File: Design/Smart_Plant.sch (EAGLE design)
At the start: 85 parts, among them IC1 NE555D, Q1 IRLML0100, Q3 2.5A/30V, Q4 MBT3904DW1T1, U10 ESP3212, U6 W25Q32FVSS, U7 FT231XS, U8 MCP73831, U9 AP2112K-3.3V, X2 MICROSD, Y3 26MHz

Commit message: Updated design files for Smart_Plant
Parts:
- removed C29, C30: 10pF, SparkFun-Capacitors:10PF-0603-50V-5%
- removed C31, C32: 270pF, esp32-thing-temp:270PF-50V-5%(0603)
- removed C33: 10nF, SparkFun-Capacitors:10NF-0603-50V-10%
- removed C34, C37, C38, C41, C48, C49, C51, C53: 0.1uF, SparkFun-Capacitors:0.1UF-0603-25V-(+80/-20%)
- removed C35: 2.4pF, esp32-thing-temp:2.4PF-0603-50V-5%
- removed C36: 5.6pF, esp32-thing-temp:5.6PF-50V-5%(0603)
- removed C39, C40: 47pF, SparkFun-Capacitors:47PF-0603-50V-5%
- removed C42: 4.7uF, SparkFun-Capacitors:4.7UF-6.3V-10%(0603)0603
- removed C43: 1.0uF, SparkFun-Capacitors:1.0UF-0805-25V-(+80/-20%)
- removed C44: 2.2uF, SparkFun-Capacitors:2.2UF-0603-10V-20%
- removed C45, C46: 4.7uF, SparkFun-Capacitors:4.7UF0603
- removed C47: 100pF, SparkFun-Capacitors:100PF-0603-50V-5%
- removed C50: 10uF, SparkFun-Capacitors:10UF-0603-6.3V-20%
- removed C52: 1.0uF, SparkFun-Capacitors:1.0UF-0603-16V-10%
- removed C56: 3.0nF, esp32-thing-temp:3.0NF-0603-50V-5%
- removed D10, D9: MBR0530, microbuilder:DIODE-SCHOTTKYSOD-123
- removed D5: BAT20J, SparkFun-DiscreteSemi:DIODE-SCHOTTKY-BAT20J
- removed D6: Yellow, SparkFun-LED:LED-YELLOW0603
- removed D7: Green, SparkFun-LED:LED-RED0603
- removed E2: ANTENNA, esp32-thing-temp:ANTENNATRACE-TUNED
- removed EINK1: EINK_24PIN_290IN, microbuilder:EINK_24PIN_290IN
- removed F2: 500mA, SparkFun-PowerIC:PTCSMD
- removed JP1: (no value), SparkFun-Connectors:USB_MICROB_PLUGCONN-11752
- removed JP3: LiPo, SparkFun-Connectors:M02JST-PTH-2
- removed L2: 2.7nH, SparkFun-Passives:INDUCTOR0603
- removed Q3: 2.5A/30V, SparkFun-DiscreteSemi:MOSFET-PCHANNELDMG2307L
- removed Q4: MBT3904DW1T1, esp32-thing-temp:MBT3904DW1T1
- removed R19, R24: 1K, SparkFun-Resistors:1KOHM-1/10W-1%(0603)
- removed R20: 2.0k, SparkFun-Resistors:2.0KOHM1/10W5%(0603)
- removed R21: DNP, SparkFun-Passives:RESISTORPTH-1/6W
- removed R22, R23: 10k, SparkFun-Resistors:10KOHM-0603-1/10W-1%
- removed R26: 10k, SparkFun-Resistors:10KOHM-1/10W-1%(0603)0603
- removed R27: DNP, microbuilder:RESISTOR0805_10MGAP
- removed S3: RESET, SparkFun-Electromechanical:SWITCH-MOMENTARY-2SMD-4.6X2.8MM
- removed S4: BTN-0, SparkFun-Electromechanical:SWITCH-MOMENTARY-2SMD-4.6X2.8MM
- removed SJ4: JUMPER-PAD-3-2OF3_NC_BY_TRACE_SMALL, SparkFun-Passives:JUMPER-PAD-3-2OF3_NC_BY_TRACE_SMALL
- removed SJ5: JUMPER-PAD-2-NC_BY_TRACE, SparkFun-Passives:JUMPER-PAD-2-NC_BY_TRACE
- removed U10: ESP3212, esp32-thing-temp:ESP3212
- removed U6: W25Q32FVSS, SparkFun-DigitalIC:W25Q32FVSS
- removed U7: FT231XS, SparkFun-DigitalIC:FT231XS
- removed U8: MCP73831, SparkFun-PowerIC:MCP73831
- removed U9: AP2112K-3.3V, SparkFun-PowerIC:V_REG_LDOSMD
- removed X2: MICROSD, microbuilder:MICROSD
- removed Y3: 26MHz, things:CRYSTAL-GROUNDED3.2X2.5
- added BT1: (no value), SparkFun-Batteries:BATTERY-20MM_PTH
- added C10, C16, C4: 10uF, rcl:C-USC0603
- added C11, C6: 100nF, rcl:C-USC0603
- added C12: 22uF, rcl:C-USC0603
- added C15: 0.1uF, rcl:C-USC0603
- added C5: 10nF, rcl:C-USC0603
- added C7: 1uF, rcl:C-USC0603
- added D1, D2, D3: SS14, SparkFun-DiscreteSemi:DIODE-SCHOTTKY-SS14
- added FPC: E-PAPER-FPC, SpaceDIY_connectors:E-PAPER-FPC
- added IC2: TLC555CDR, linear:NE555D
- added IC3: AHT20, SamacSys_Parts:AHT20
- added IC4: TP4056, TP4056:TP4056
- added J1: (no value), SparkFun-Connectors:CONN_02
- added J3: (no value), pinhead:PINHD-1X4
- added LED1: Red, SpaceDIY_semiconductors:LED0603
- added LED2: Green, SpaceDIY_semiconductors:LED0603
- added Q2: ALS-PT19-315C, SparkFun-DiscreteSemi:PHOTOTRANSISTORPT17-21C-L41-TR8
- added R14, R7: 10k, rcl:R-US_R0603
- added R17: 220, rcl:R-US_R0603
- added R4: 33k, rcl:R-US_R0603
- added R5: 1K, rcl:R-US_R0603
- added R6: 1k, rcl:R-US_R0603
- added R8: 1M, rcl:R-US_R0603
- added R9: 10K, rcl:R-US_R0603
- added S1: Flash, SpaceDIY_electromechanical:MOMENTARY-SWITCH-SPST-SMD-5.2MM-TALL
- added S2: Reset, SpaceDIY_electromechanical:MOMENTARY-SWITCH-SPST-SMD-5.2MM-TALL
- added T1: MMBT2222A, JLC PCB Basic Parts_loc:T_NPN_MMBT2222A-1P_CHANGJ_SOT23-BEC
- added T2: LBSS84LT1G, JLC PCB Basic Parts_loc:T_P-MOSFET_LBSS84LT1G_LRC_SOT23-GSD
- added TP1, TP2: TPB1,27, testpad:TPB1,27
- added U1: ESP-32S, esp32:ESP-32S
- C1: value 0.1uF -> 10uF; device SparkFun-Capacitors:0.1UF-0603-25V-(+80/-20%) -> rcl:C-USC0603
- C13, C14, C17, C18, C19, C25, C27, C28, C9: device microbuilder:CAP_CERAMIC0805-NOOUTLINE -> rcl:C-USC0603
- C2: value 0.1uF -> 4.7uF; device SparkFun-Capacitors:0.1UF-0603-25V-(+80/-20%) -> rcl:C-USC0603
- C26: value 4.7uF/25V -> 4.7uF; device microbuilder:CAP_CERAMIC0805-NOOUTLINE -> rcl:C-USC0603
- C3: value 0.1uF -> 0.47nF; device SparkFun-Capacitors:0.1UF-0603-25V-(+80/-20%) -> rcl:C-USC0603
- C8: value 10uF/10V+ -> 10uF; device microbuilder:CAP_CERAMIC0805-NOOUTLINE -> rcl:C-USC0603
- D4: value MBR0530 -> LL4148; device microbuilder:DIODE-SCHOTTKYSOD-123 -> SpaceDIY_semiconductors:LL4148
- IC1: value NE555D -> AMS1117-3.3; device linear:NE555D -> SparkFun-IC-Power:V_REG_LD1117VXXLD1117-SMD
- R1, R12, R15: value 27 -> 10k; device SparkFun-Resistors:27OHM1/10W1%(0603)0603-RES -> rcl:R-US_R0603
- R10: device SparkFun-Resistors:10KOHM-1/10W-1%(0603)0603 -> rcl:R-US_R0603
- R11: value 20k -> 1k; device SparkFun-Resistors:20KOHM-0603-1/10W-1% -> rcl:R-US_R0603
- R13: value 0.47ohm -> 0.47; device microbuilder:RESISTOR0805_10MGAP -> rcl:R-US_R0603
- R16: device SparkFun-Resistors:10KOHM-0603-1/10W-1% -> rcl:R-US_R0603
- R2: value 27 -> 330R; device SparkFun-Resistors:27OHM1/10W1%(0603)0603-RES -> rcl:R-US_R0603
- R3: value 27 -> 1.5k; device SparkFun-Resistors:27OHM1/10W1%(0603)0603-RES -> rcl:R-US_R0603
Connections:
- removed net 0: Q4Q2.C, R26.1, S4.2, U10.(ADC2:1/TOUCH1/RTC11/CLK_OUT1)GPIO0
- removed net 12: U10.(GPIO12/ADC2:5/TOUCH5/RTC15/SPIQ)MTDI
- removed net 19: U10.(VSPIQ/HS2_DATA2)GPIO19
- removed net 21: U10.(VSPIHD/HS2_CMD)GPIO21
- removed net 22: U10.(VSPIWP/HS2_CLK)GPIO22
- removed net 25: U10.(DAC1/ADC2:8/RTC6)GPIO25
- removed net 26: U10.(DAC2/ADC2:9/RTC7)GPIO26
- removed net 27: U10.(ADC2:7/TOUCH7/RTC17)GPIO27
- removed net 3.3V_F: C41.1, U7.!RESET, U7.3V3OUT, U7.VCCIO
- removed net 32: U10.32K_XP(GPIO32/ADC1:4/TOUCH9/RTC9)
- removed net 33: U10.32K_XN(GPIO33/ADC1:5/TOUCH8/RTC8)
- removed net 34: U10.VDET_1(GPI34/ADC1:6)
- removed net 35: U10.VDET_2(GPI35/ADC1:7)
- removed net 36: C31.2, U10.SENSOR_VP(GPI36/ADC1:0/RTC0)
- removed net 37: C31.1, U10.SENSOR_CAPP(GPI37/ADC1:1/RTC1)
- removed net 38: C32.1, U10.SENSOR_CAPN(GPI38/ADC1:2/RTC2)
- removed net 39: C32.2, U10.SENSOR_VN(GPI39/ADC1:3/RTC3)
- removed net 3V3: C44.1, C47.1, C48.1, C49.1, C50.1, C51.1, C53.1, C8.2, EINK1.VCI, EINK1.VDDIO, L3.2, R10.2, R24.1, R26.2, SJ4.3, U10.VDD3P3_CPU, U10.VDD3P3_RTC, U10.VDDA, U10.VDDA3P3, U9.OUT, X2.SD_VDD
- removed net CAP_10N1: C33.2, C56.1, R11.2, U10.CAP1
- removed net CHIP_PU: Q4Q1.C, R10.1, S3.2, U10.CHIP_PU
- removed net D+: C39.1, JP1.D+, R15.1
- removed net D-: C40.1, JP1.D-, R12.1
- removed net DTR: Q4Q2.E, R22.1, U7.!DTR
- removed net FLASH_SCK: U10.(GPIO6/SPICLK/HS1_CLK/U1CTS)SD_CLK, U6.SCK
- removed net FLASH_SCS: U10.(GPIO11/SPICSO/HS1_CMD/U1RTS)SD_CMD, U6.!CS!
- removed net FLASH_SDI: U10.(GPIO8/SPID/HS1_DATA1)SD_DATA1, U6.SI(D0)
- removed net FLASH_SDO: U10.(GPIO7/SPI1/HS1_DATA0)SD_DATA0, U6.SO(D1)
- removed net FLASH_SHD: U10.(GPIO9/SPIHD/HS1_DATA2/U1RX)SD_DATA2, U6.!HOLD!(D3)
- removed net FLASH_SWP: U10.(GPIO10/SPIWP/HS1_DATA3/U1TX)SD_DATA3, U6.!WP!(D2)
- removed net FLASH_VDD: C52.1, SJ4.1, U10.VDD3P3_SDIO
- removed net LNA_IN1: C36.1, L2.1, U10.LNA_IN
- removed net MISO_SD: U10.(ADC2:2/TOUCH2/RTC12/SPIWP)GPIO2, X2.DATA_OUT
- removed net MOSI_SD: U10.(GPIO15/ADC2:3/TOUCH3/RTC13/SPICSO/U0RTS)MTDO, X2.DATA_IN
- removed net N$19: D6.A, R19.2
- removed net N$20: D6.C, U8.STAT
- removed net N$21: R21.2, SJ5.2, U8.PROG
- removed net N$22: R20.2, SJ5.1
- removed net N$23: Q4Q1.B, R22.2
- removed net N$24: Q4Q2.B, R23.2
- removed net N$25: C29.2, U10.XTAL_P, Y3.1
- removed net N$26: C30.2, U10.XTAL_N, Y3.2
- removed net N$27: D7.A, R24.2
- removed net N$30: C56.2, R11.1, U10.CAP2
- removed net RTS: Q4Q1.E, R23.1, U7.!RTS
- removed net SCLK_SD: U10.(GPIO14/ADC2:6/TOUCH6/RTC16/SPICLK)MTMS, X2.SCLK
- removed net SDCS_SD: U10.(GPIO13/ADC2:4/TOUCH4/RTC14/SPID/U0CTS)MTCK, X2.CS
- removed net SHIELD: JP1.SHIELD
- removed net TRACE_ANT1: C35.1, C36.2, E2.SIGNAL
- removed net TSCL: EINK1.TSCL
- removed net TSDA: EINK1.TSDA
- removed net U0RXD: U10.(GPIO3/CLK_OUT2/HS2_DATA0)U0RXD, U7.TXD
- removed net U0TXD: U10.(GPIO1/CLK_OUT3/HS2_DATA1)U0TXD, U7.RXD
- removed net VUSB-RAW: C37.1, F2.1, JP1.VCC
- removed net V_BATT: C45.1, JP3.2, Q3.D, U8.VBAT
- removed net V_USB: C38.1, C42.1, C46.1, D5.A, F2.2, Q3.G, R16.2, R19.1, U7.VCC, U8.VIN
- new net 3.3V: C10.1, C11.1, C12.1, C2.1, FPC.15, FPC.16, IC1.OUT, J3.1, L3.2, R10.1, R12.1, R9.2, T2.S, U1.3V3
- new net IO0: R12.2, S1.2, U1.IO0
- new net LIGHT: Q2.E, R14.1, U1.IO33
- new net MOISTURE: C7.1, D4.C, R8.1, U1.IO32
- new net N$1: IC4.PROG, R4.2
- new net N$10: C15.1, C16.1, IC3.VDD, R17.2
- new net N$2: IC4.!STDBY, R6.2
- new net N$3: LED1.C, R5.1
- new net N$4: LED2.C, R6.1
- new net N$7: IC2.DIS, R2.2, R3.1
- new net N$8: C5.2, IC2.CV
- new net N$9: R10.2, T1.C, T2.G
- new net OUT: IC2.Q, R7.2, TP1.TP
- new net PROBE: D4.A, R7.1
- new net RST: R9.1, S2.2, U1.EN
- new net RX: J3.4, U1.U0RXD
- new net SCL: IC3.SCL, R15.2, U1.IO22
- new net SDA: IC3.SDA, R16.2, U1.IO21
- new net SENS: R11.1, U1.IO16
- new net TX: J3.3, U1.U0TXD
- new net VBAT: BT1.+, C4.1, C8.1, IC1.IN, IC4.BAT
- new net VSENS: C6.1, IC2.R, IC2.V+, Q2.C, R15.1, R16.1, R17.1, R2.1, T2.D, TP2.TP
- net BUSY: now also FPC.9, U1.IO25; no longer EINK1.BUSY, U10.(ADC2:0/TOUCH0/RTC10/SPIHD)GPIO4
- net DC: now also FPC.11, U1.IO27; no longer EINK1.D/C#, U10.(HS1_DATA5)GPIO17
- net DISPCS: now also FPC.12, U1.IO15; no longer EINK1.CS#, U10.(VSPICS0/HS1_DATA6)GPIO5
- net GDR: now also FPC.2, R1.1; no longer EINK1.GDR
- net GND: now also BT1.-, C1.2, C10.2, C11.2, C12.2, C15.2, C16.2, C2.2, C3.2, C4.2, C5.1, C6.2, C7.2, C8.2, D2.C, FPC.17, FPC.8, IC1.GND, IC2.GND, IC3.GND, IC4.CE, IC4.GND, J1.2, J3.2, R1.2, R14.2, R4.1, R8.2, S1.1, S2.1, T1.E, U1.GND@1, U1.GND@2, U1.GND@3, U1.GND@4; no longer C29.1, C30.1, C33.1, C34.2, C35.2, C37.2, C38.2, C39.2, C40.2, C41.2, C42.2, C43.2, C44.2, C45.2, C46.2, C47.2, C48.2, C49.2, C50.2, C51.2, C52.2, C53.2, C8.1, D4.C, D7.C, E2.GND, EINK1.BSI, EINK1.VSS, JP1.GND, JP3.1, L2.2, R16.1, R20.1, R21.1, R27.2, S3.1, S4.1, U10.GND, U6.GND, U7.GND@16, U7.GND@6, U8.VSS, U9.GND, X2.GND@1, X2.GND@2, X2.GND@3, Y3.GND
- net MOSI: now also FPC.14, U1.IO14; no longer EINK1.SDIO, U10.GPIO23
- net N$11: now also FPC.5; no longer EINK1.VSH2
- net N$12: now also FPC.18; no longer EINK1.VDD
- net N$13: now also FPC.20; no longer EINK1.VSH1
- net N$14: now also FPC.22; no longer EINK1.VSL
- net N$15: now also FPC.24; no longer EINK1.VCOM
- net N$16: now also D2.A, D3.C; no longer D4.A, D9.C
- net N$17: now also D1.A; no longer D10.A
- net N$18: now also R11.2, T1.B; no longer R15.2, U7.USBDP
- net N$31: now also FPC.4; no longer EINK1.VGL/NC
- net N$32: now also FPC.19; no longer EINK1.VPP
- net N$5: now also C3.1, IC2.THR, IC2.TR, R3.2; no longer C34.1, SJ4.2, U6.VCC
- net N$6: now also IC4.!CHRG, R5.2; no longer R12.2, U7.USBDM
- net RESE: now also FPC.3; no longer EINK1.RESE, R27.1
- net RESET: now also FPC.10, U1.IO26; no longer EINK1.RES#, U10.(HS1_DATA4)GPIO16
- net SCLK: now also FPC.13, U1.IO13; no longer EINK1.SCK, U10.(VSPICLK/HS1_DATA7)GPIO18
- net VGH: now also D1.C, FPC.21; no longer D10.C, EINK1.VGH
- net VGL: now also D3.A, FPC.23; no longer D9.A, EINK1.VGL
- net VIN: now also C1.1, IC4.TEMP, IC4.VCC, J1.1, LED1.A, LED2.A; no longer C43.1, D5.C, Q3.S, U9.EN, U9.IN
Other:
- note added: "Battery charger"
- note added: "Capacitive moisture sensor"
- note added: "High switch for power supply"
- note added: "Light sensor"
- note added: "Microcontroller"
- note added: "Notes: - Battery: LiR2032"
- note added: "Power reg"
- note added: "Reset & Flash switches"
- note added: "Serial port"
- note added: "Temperature & humidity sensor"
- note added: "eInk Display"

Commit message: Update design files
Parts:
- removed BT1: (no value), SparkFun-Batteries:BATTERY-20MM_PTH
- removed J3: (no value), pinhead:PINHD-1X4
- added J2: USBC-6P, SpaceDIY_connectors:USBC-6P
- added J4: (no value), SparkFun-Connectors:CONN_02-JST-2-PTH-NO_SILK
- added J5: (no value), SparkFun-Connectors:CONN_04PTH
- added R18: 240k, rcl:R-US_R0603
- added R19: 1M, rcl:R-US_R0603
- R4: value 33k -> 1.2k
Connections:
- new net BATTERY: R18.1, R19.2, U1.IO35
- net 3.3V: now also J5.1; no longer J3.1
- net GND: now also J2.GND, J4.1, J5.2, R18.2; no longer BT1.-, J3.2
- net RX: now also J5.4; no longer J3.4
- net TX: now also J5.3; no longer J3.3
- net VBAT: now also J4.2, R19.1; no longer BT1.+
- net VIN: now also J2.VBUS
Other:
- note added: "Battery monitoring"
- moved on the sheet: Q2, R14

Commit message: Resistors charger note
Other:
- note added: "R4 [k] - IBAT [mA] ------------------------ 10 - 130 5 - 250 4 - 300 3 - 400 2 - 580 1.66 - 690 1.5 - 780 1.33 - 900 1.2 - 1000"
- note removed: "Notes: - Battery: LiR2032"
- moved on the sheet: J1
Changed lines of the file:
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@@
 <text x="167.64" y="73.66" size="2.54" layer="95">Reset &amp; Flash switches</text>
 <wire x1="152.4" y1="96.52" x2="5.08" y2="96.52" width="0.254" layer="95" style="longdash"/>
-<text x="162.56" y="22.86" size="1.778" layer="94" align="top-left">Notes:
-- Battery: LiR2032 </text>
+<text x="7.62" y="43.18" size="1.778" layer="94" align="top-left">R4 [k] - IBAT [mA]
+------------------------
+10 - 130
+5 - 250
+4 - 300
+3 - 400
+2 - 580
+1.66 - 690
+1.5 - 780
+1.33 - 900
+1.2 - 1000
+</text>
 <wire x1="93.98" y1="175.26" x2="93.98" y2="96.52" width="0.254" layer="95" style="longdash"/>
 <wire x1="152.4" y1="78.74" x2="213.36" y2="78.74" width="0.254" layer="95" style="longdash"/>
@@
 <attribute name="VALUE" x="113.284" y="130.429" size="1.778" layer="96" rot="MR0"/>
 </instance>
-<instance part="J1" gate="G$1" x="33.02" y="43.18" smashed="yes" rot="MR180">
-<attribute name="VALUE" x="30.48" y="48.006" size="1.778" layer="96" font="vector" rot="MR180"/>
-<attribute name="NAME" x="30.48" y="37.592" size="1.778" layer="95" font="vector" rot="MR180"/>
-</instance>
-<instance part="GND9" gate="1" x="43.18" y="33.02" smashed="yes">
-<attribute name="VALUE" x="40.64" y="30.48" size="1.778" layer="96"/>
+<instance part="J1" gate="G$1" x="38.1" y="43.18" smashed="yes" rot="MR180">
+<attribute name="VALUE" x="35.56" y="48.006" size="1.778" layer="96" font="vector" rot="MR180"/>
+<attribute name="NAME" x="35.56" y="37.592" size="1.778" layer="95" font="vector" rot="MR180"/>
+</instance>
+<instance part="GND9" gate="1" x="48.26" y="30.48" smashed="yes">
+<attribute name="VALUE" x="45.72" y="27.94" size="1.778" layer="96"/>
 </instance>
 <instance part="IC1" gate="G$1" x="68.58" y="81.28" smashed="yes">
@@
 <segment>
 <pinref part="J1" gate="G$1" pin="2"/>
-<wire x1="40.64" y1="40.64" x2="43.18" y2="40.64" width="0.1524" layer="91"/>
-<wire x1="43.18" y1="40.64" x2="43.18" y2="35.56" width="0.1524" layer="91"/>
+<wire x1="45.72" y1="40.64" x2="48.26" y2="40.64" width="0.1524" layer="91"/>
+<wire x1="48.26" y1="40.64" x2="48.26" y2="33.02" width="0.1524" layer="91"/>
 <pinref part="GND9" gate="1" pin="GND"/>
 </segment>
@@
 <wire x1="60.96" y1="43.18" x2="53.34" y2="43.18" width="0.1524" layer="91"/>
 <wire x1="53.34" y1="43.18" x2="53.34" y2="40.64" width="0.1524" layer="91"/>
-<wire x1="53.34" y1="43.18" x2="40.64" y2="43.18" width="0.1524" layer="91"/>
+<wire x1="53.34" y1="43.18" x2="45.72" y2="43.18" width="0.1524" layer="91"/>
 <junction x="53.34" y="43.18"/>
 <pinref part="J1" gate="G$1" pin="1"/>

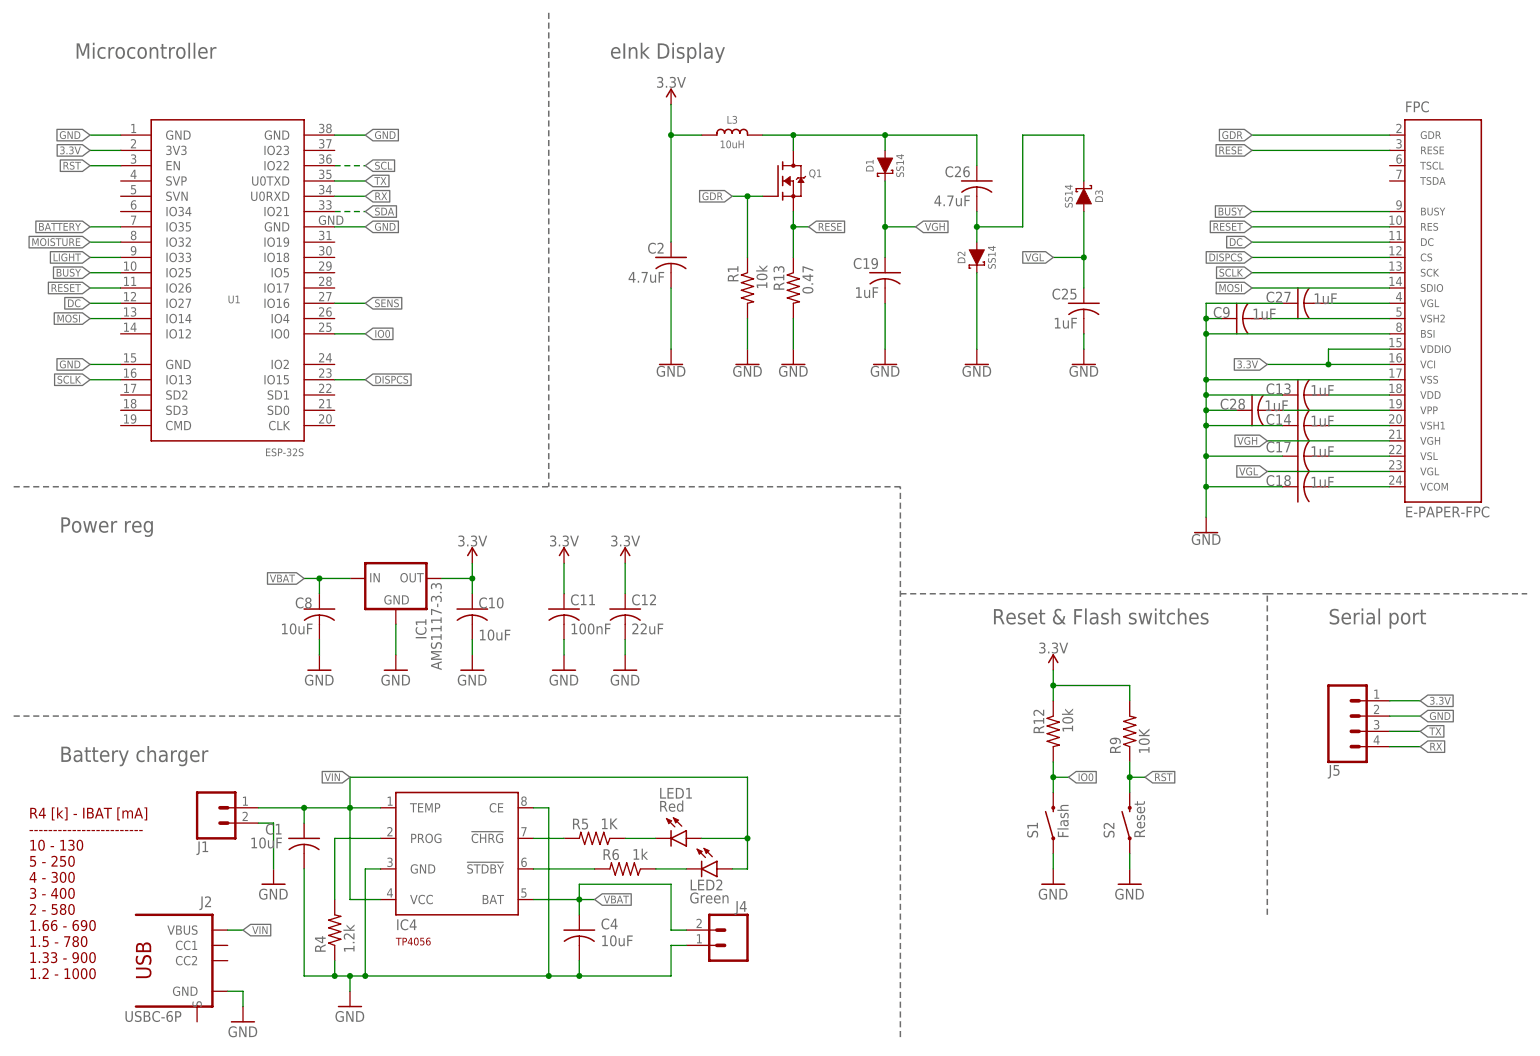
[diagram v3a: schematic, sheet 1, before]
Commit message: Added designs for V1R2
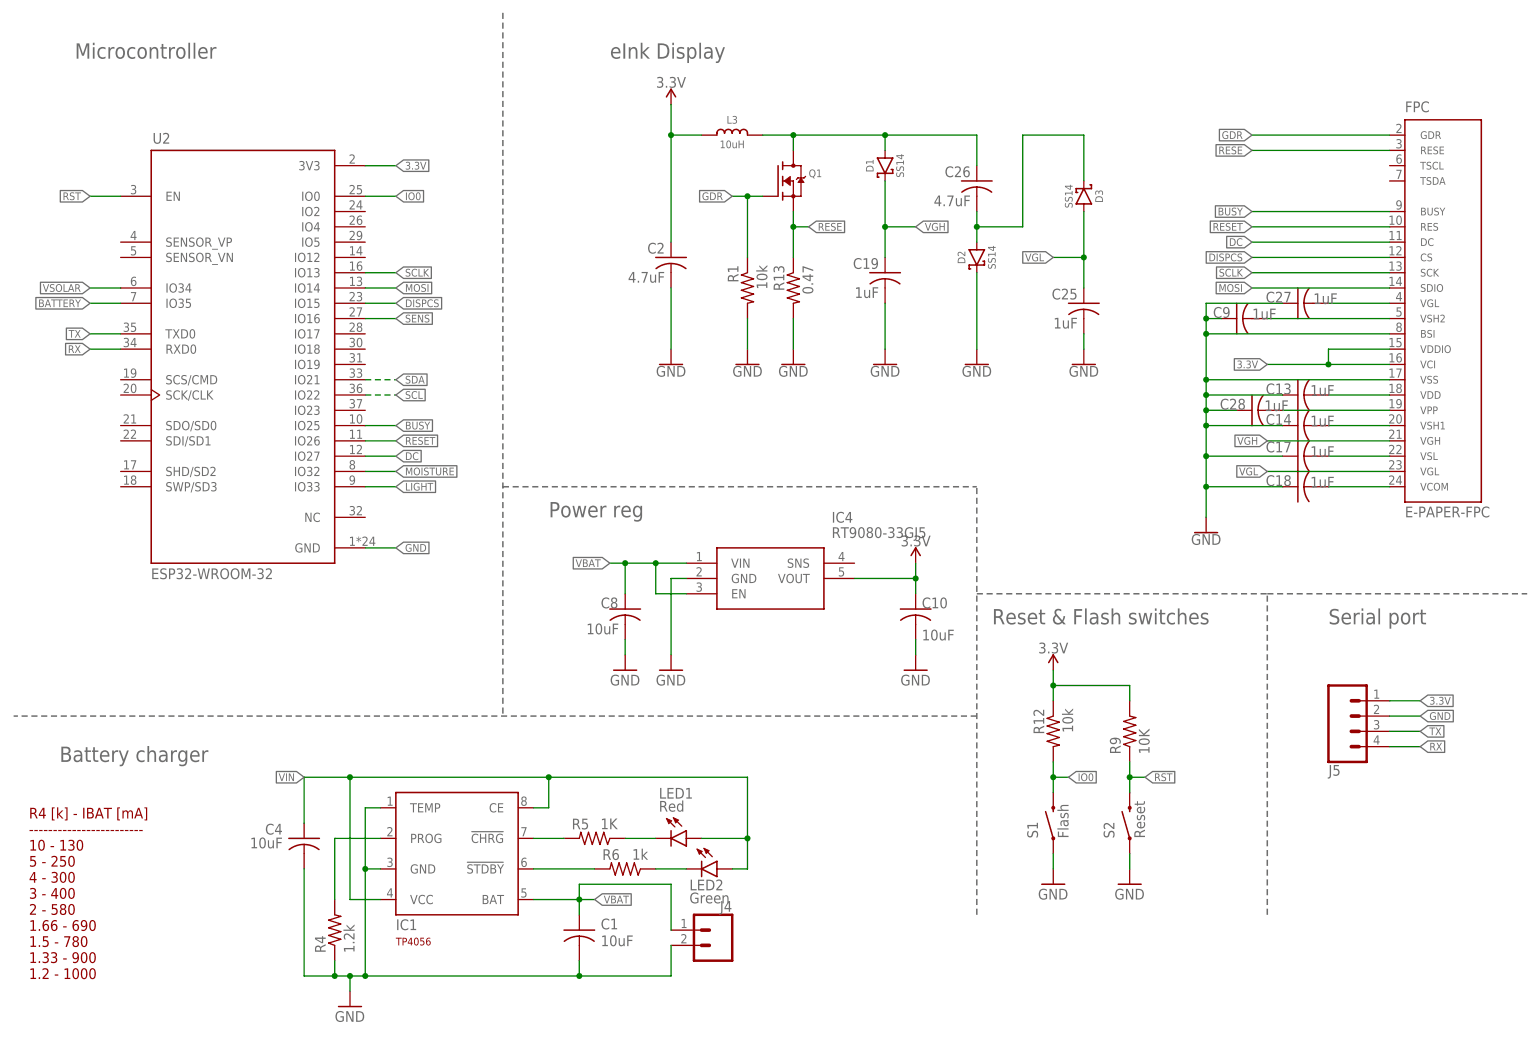
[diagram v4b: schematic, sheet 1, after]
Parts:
- removed C11: 100nF, rcl:C-USC0603
- removed C12: 22uF, rcl:C-USC0603
- removed J2: USBC-6P, SpaceDIY_connectors:USBC-6P
- removed Q2: ALS-PT19-315C, SparkFun-DiscreteSemi:PHOTOTRANSISTORPT17-21C-L41-TR8
- removed U1: ESP-32S, esp32:ESP-32S
- added D5, D6: SS14, SpaceDIY_semiconductors:DIODE-SCHOTTKYSS14
- added J6: USB-C, SparkFun-Connectors:USB_C_4-LAYER-ISOLATED
- added LDR: PHOTOCELLPTH, SparkFun-Sensors:PHOTOCELLPTH
- added R20: 1M, rcl:R-US_R0603
- added R21: 240k, rcl:R-US_R0603
- added U2: ESP32-WROOM-32, ESP32-WROOM-32:ESP32-WROOM-32
- D1, D2, D3: device SparkFun-DiscreteSemi:DIODE-SCHOTTKY-SS14 -> SpaceDIY_semiconductors:DIODE-SCHOTTKYSS14
- IC1: value AMS1117-3.3 -> TP4056; device SparkFun-IC-Power:V_REG_LD1117VXXLD1117-SMD -> TP4056:TP4056
- IC4: value TP4056 -> RT9080-33GJ5; device TP4056:TP4056 -> SamacSys_Parts:RT9080-33GJ5; LCSC (none) -> C841192
- J4: device SparkFun-Connectors:CONN_02-JST-2-PTH-NO_SILK -> SpaceDIY_connectors:CONN_02-JST-2MM-SMT; LCSC (none) -> C3029440
- R18: value 240k -> 1M
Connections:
- removed net N$2 (its old number): IC4.!STDBY, R6.2
- new net D+: J6.D+
- new net D-: J6.D-
- new net N$4: IC1.PROG, R4.2
- new net N$46: D6.A, J1.1, R20.1
- new net VSOLAR: R20.2, R21.2, U2.IO34
- new net V_USB: D5.A, J6.VBUS
- net 3.3V: now also IC4.VOUT, U2.3V3; no longer C11.1, C12.1, IC1.OUT, U1.3V3
- net BATTERY: now also U2.IO35; no longer U1.IO35
- net BUSY: now also U2.IO25; no longer U1.IO25
- net DC: now also U2.IO27; no longer U1.IO27
- net DISPCS: now also U2.IO15; no longer U1.IO15
- net GND: now also IC1.TEMP, J6.GND, R21.1, U2.GND; no longer C11.2, C12.2, IC4.CE, J2.GND, U1.GND@1, U1.GND@2, U1.GND@3, U1.GND@4
- net IO0: now also U2.IO0; no longer U1.IO0
- net LIGHT: now also LDR.P$1, U2.IO33; no longer Q2.E, U1.IO33
- net MOISTURE: now also U2.IO32; no longer U1.IO32
- net MOSI: now also U2.IO14; no longer U1.IO14
- net N$1: now also IC1.!STDBY, R6.2; no longer IC4.PROG, R4.2
- net N$6: now also IC1.!CHRG; no longer IC4.!CHRG
- net RESET: now also U2.IO26; no longer U1.IO26
- net RST: now also U2.EN; no longer U1.EN
- net RX: now also U2.RXD0; no longer U1.U0RXD
- net SCL: now also U2.IO22; no longer U1.IO22
- net SCLK: now also U2.IO13; no longer U1.IO13
- net SDA: now also U2.IO21; no longer U1.IO21
- net SENS: now also U2.IO16; no longer U1.IO16
- net TX: now also U2.TXD0; no longer U1.U0TXD
- net VBAT: now also C1.1, IC1.BAT, IC4.EN, IC4.VIN; no longer C4.1, IC1.IN, IC4.BAT
- net VIN: now also C4.1, D5.C, D6.C, IC1.CE, IC1.VCC; no longer C1.1, IC4.TEMP, IC4.VCC, J1.1, J2.VBUS
- net VSENS: now also LDR.P$2; no longer Q2.C
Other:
- note added: "Input power/data connectors"
- moved on the sheet: C1, C10, C4, C8, J4, R10, R11, R14, R18, R19, T1, T2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

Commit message: SoC first draft
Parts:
- removed LDR: PHOTOCELLPTH, SparkFun-Sensors:PHOTOCELLPTH
- removed R12: 10k, rcl:R-US_R0603
- removed R19: 1M, rcl:R-US_R0603
- removed R9: 10K, rcl:R-US_R0603
- added C11: 100nF, rcl:C-USC0603
- added C20: 2.4pF, esp32-thing-temp:2.4PF-0603-50V-5%
- added C21: 5.6pF, esp32-thing-temp:5.6PF-50V-5%(0603)
- added C40: 1uF, rcl:C-USC0603
- added C46, C48, C55, C57, C62, C63: 1uF, microbuilder:CAP_CERAMIC_0402NO
- added C47, C52, C53, C54, C56, C58: 0.1uF, microbuilder:CAP_CERAMIC_0402NO
- added C49: 22uF, microbuilder:CAP_CERAMIC0805-NOOUTLINE
- added C59, C60: 16pF, microbuilder:CAP_CERAMIC_0402NO
- added C61: 1uF, SpaceDIY_passive_components:C0402
- added E2: ANTENNA, esp32-thing-temp:ANTENNATRACE-TUNED
- added IC5: LC709203F/MH, adafruit_sensor:LC709203F/MH
- added IC6: VEML7700-TR, SpaceDIY_sensors:LIGHT_SENSOR
- added L2: 2.7nH, SparkFun-Passives:INDUCTOR0603
- added L5: 2nH, microbuilder:RESISTOR_0402NO
- added R29: 0, microbuilder:RESISTOR_0402NO
- added R30: 1Meg, microbuilder:RESISTOR_0402NO
- added R31: 10K, SpaceDIY_passive_components:R0402
- added X5: ESP32-S3QFN54, adafruit_wireless:ESP32-S3QFN54
- added Y2: 40MHz, microbuilder:CRYSTAL_2X1.6MM
- R14: value 10k -> 1M
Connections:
- new net !RESET: C61.1, R31.2, S2.2, X5.CHIP_PU
- new net A2: X5.IO9
- new net A3: X5.IO8
- new net IO10_DBLTAP: C62.1, R30.2, X5.IO10
- new net LNA_IN1: C21.1, L2.1, X5.LNA_IN
- new net MISO: X5.IO37
- new net N$53: C59.1, X5.XTAL_P, Y2.2
- new net N$54: C60.1, R29.1, Y2.1
- new net N$55: R29.2, X5.XTAL_N
- new net NEOPIX: X5.MTCK
- new net NEOPIX_PWR: X5.IO38
- new net SCK: X5.IO36
- new net SCL1: X5.MTD0
- new net SDA1: X5.MTDI
- new net TRACE_ANT1: C20.1, C21.2, E2.SIGNAL
- new net VDD3P3: C47.1, L5.2, X5.VDD3P3@0, X5.VDD3P3@1
- new net VDD_SPI: C54.1, C55.1, X5.VDD_SPI
- net 3.3V: now also C46.1, C48.1, C49.1, C52.1, C53.1, C56.1, C57.1, C58.1, C63.1, L5.1, R31.1, X5.IO21, X5.VDD3P3_CPU, X5.VDD3P3_RTC, X5.VDDA@0, X5.VDDA@1; no longer R12.1, R9.2
- net BATTERY: now also R14.2, X5.IO18; no longer R19.2
- net D+: now also X5.IO20
- net D-: now also X5.IO19
- net GND: now also C11.2, C20.2, C40.2, C46.2, C47.2, C48.2, C49.2, C52.2, C53.2, C54.2, C55.2, C56.2, C57.2, C58.2, C59.2, C60.2, C61.2, C62.2, C63.2, E2.GND, IC5.TEST, IC5.VSS, IC6.GND, L2.2, R30.1, X5.GND; no longer R14.2
- net IO0: now also X5.IO0; no longer R12.2
- net LIGHT: no longer LDR.P$1, R14.1
- net MOISTURE: now also X5.IO17
- net MOSI: now also X5.IO35
- net RST: no longer R9.1, S2.2
- net RX: now also X5.U0RXD
- net SCL: now also IC5.SCL, IC6.SCL, X5.IO6
- net SDA: now also IC5.SDA, IC6.SDA, X5.IO7
- net SENS: now also X5.IO4
- net TX: now also X5.U0TXD
- net VBAT: now also C40.1, IC5.VDD, R14.1; no longer R19.1
- net VSENS: now also C11.1, IC6.VDD; no longer LDR.P$2
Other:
- note removed: "Reset & Flash switches"
